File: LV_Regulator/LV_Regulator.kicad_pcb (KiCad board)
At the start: 4 copper layers, 150 x 100 mm, 204 parts, among them IC1 UCC12040DVE, IC2 MIC29152WU, IC3 MIC29152WU, J1 430450400, J2 430450400, J3 430450800, J4 430450800, J5 SWD, J6 2169890001, K1 41.52.9.005.0010, Q1 BC807, U1 ADM2483xRW, U2 STM32F103C8Tx, U3 25CSM04xxSN, U4 BQ25858QWRRVRQ1, U5 CSD19506KTT, U6 CSD19506KTT, U7 CSD19506KTT, U8 CSD19506KTT, Y1 32.768kHz, Y2 8MHz

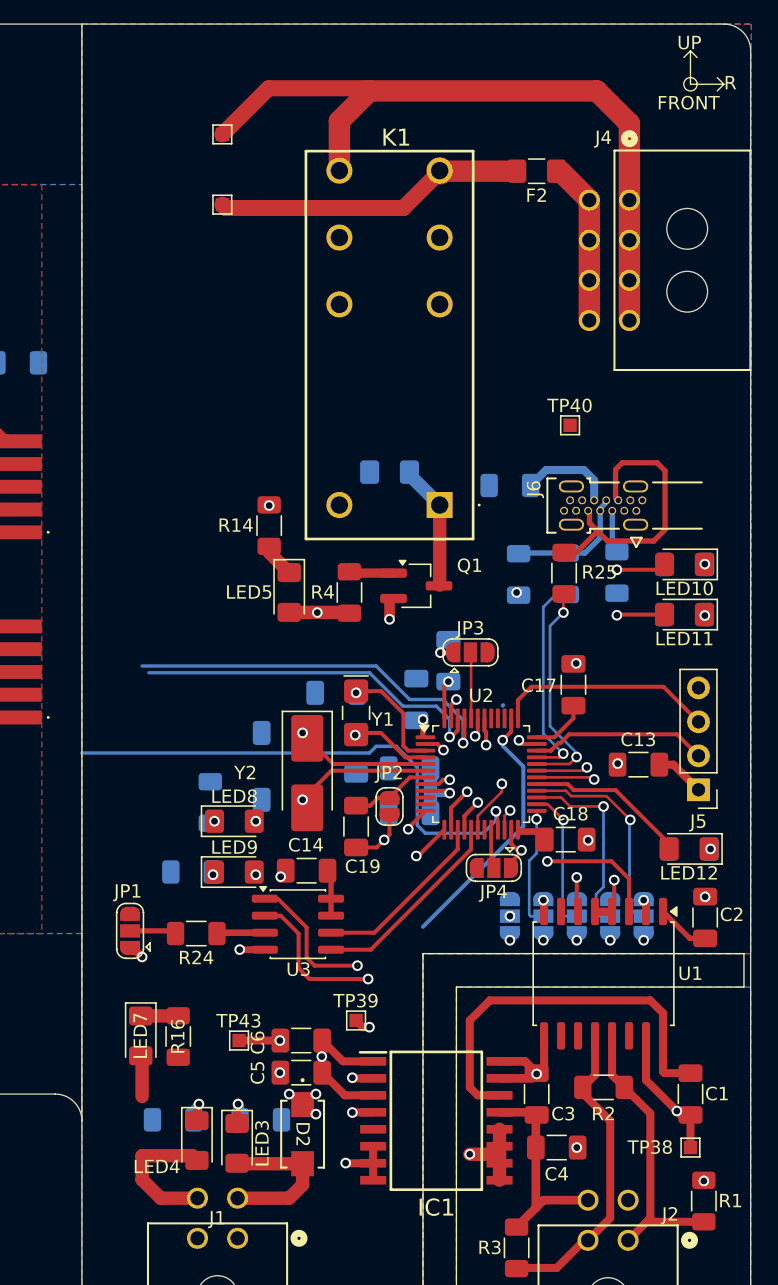
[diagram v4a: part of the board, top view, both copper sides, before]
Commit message: Small corrections to the control part of LV_Regulatoe
Changes to the PCB.
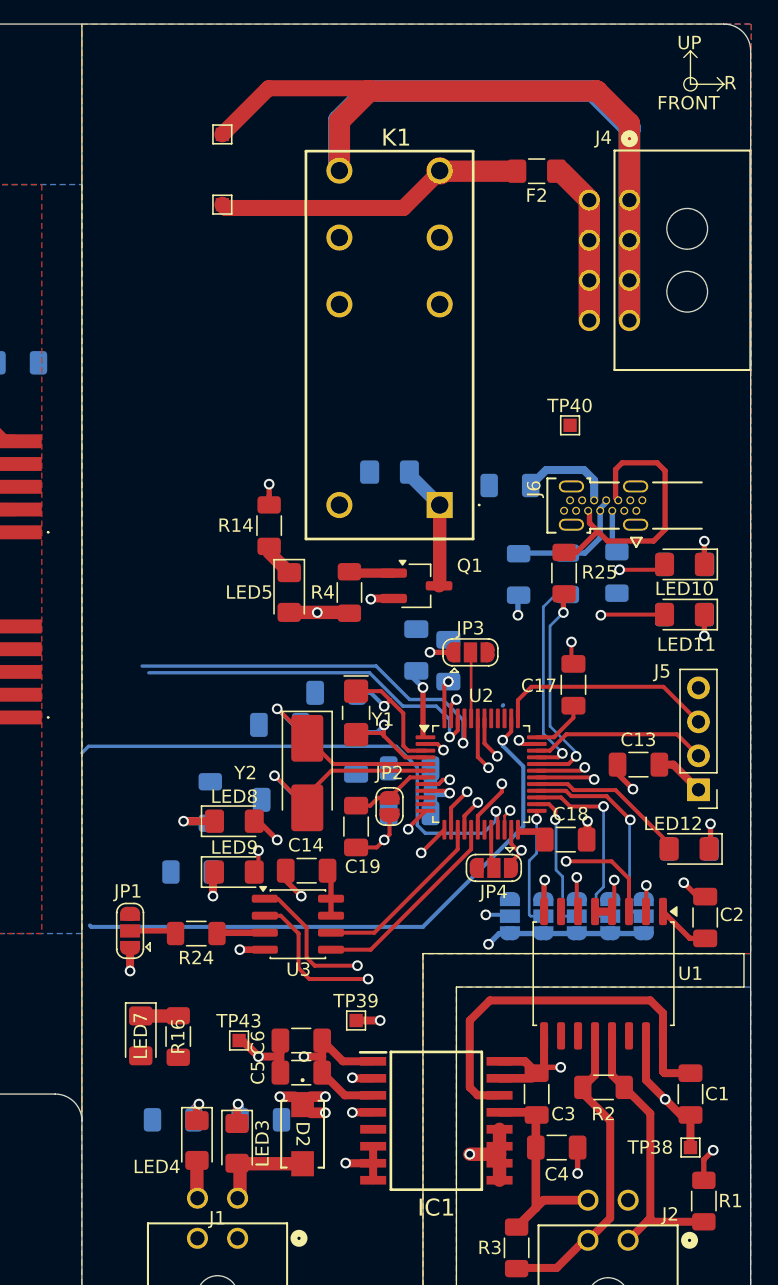
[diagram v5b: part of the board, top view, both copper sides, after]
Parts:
- moved C25 3.70 mm to (206.0, 90.8)
- moved C21 0.63 mm to (195.8, 96.4)
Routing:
- net BAT-: track 54.6 -> 96.6 mm
- net CE_N: track 21.5 -> 46.4 mm
- net GND: track 41.6 -> 63.2 mm, vias 27 -> 26
- net VBAT: track 47.4 -> 62.1 mm, vias 9 -> 5
- net 3V3_EXT: track 10.8 -> 2.84 mm
- net +5V: track 13.0 -> 20.3 mm
- net GND_ISO: track 25.3 -> 31.7 mm
- net HSC_OUT: track 10.6 -> 16.9 mm
- net HSC_IN: track 9.63 -> 15.5 mm
- net 5V_EXT: track 11.8 -> 7.33 mm
- net Net-(LED8-K): track 0.00 -> 4.37 mm
- net Net-(LED9-K): track 0.00 -> 3.67 mm
- net LSC_OUT: track 6.00 -> 9.15 mm
- net LSC_IN: track 8.46 -> 11.5 mm
- net ADR1: track 9.53 -> 12.0 mm
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
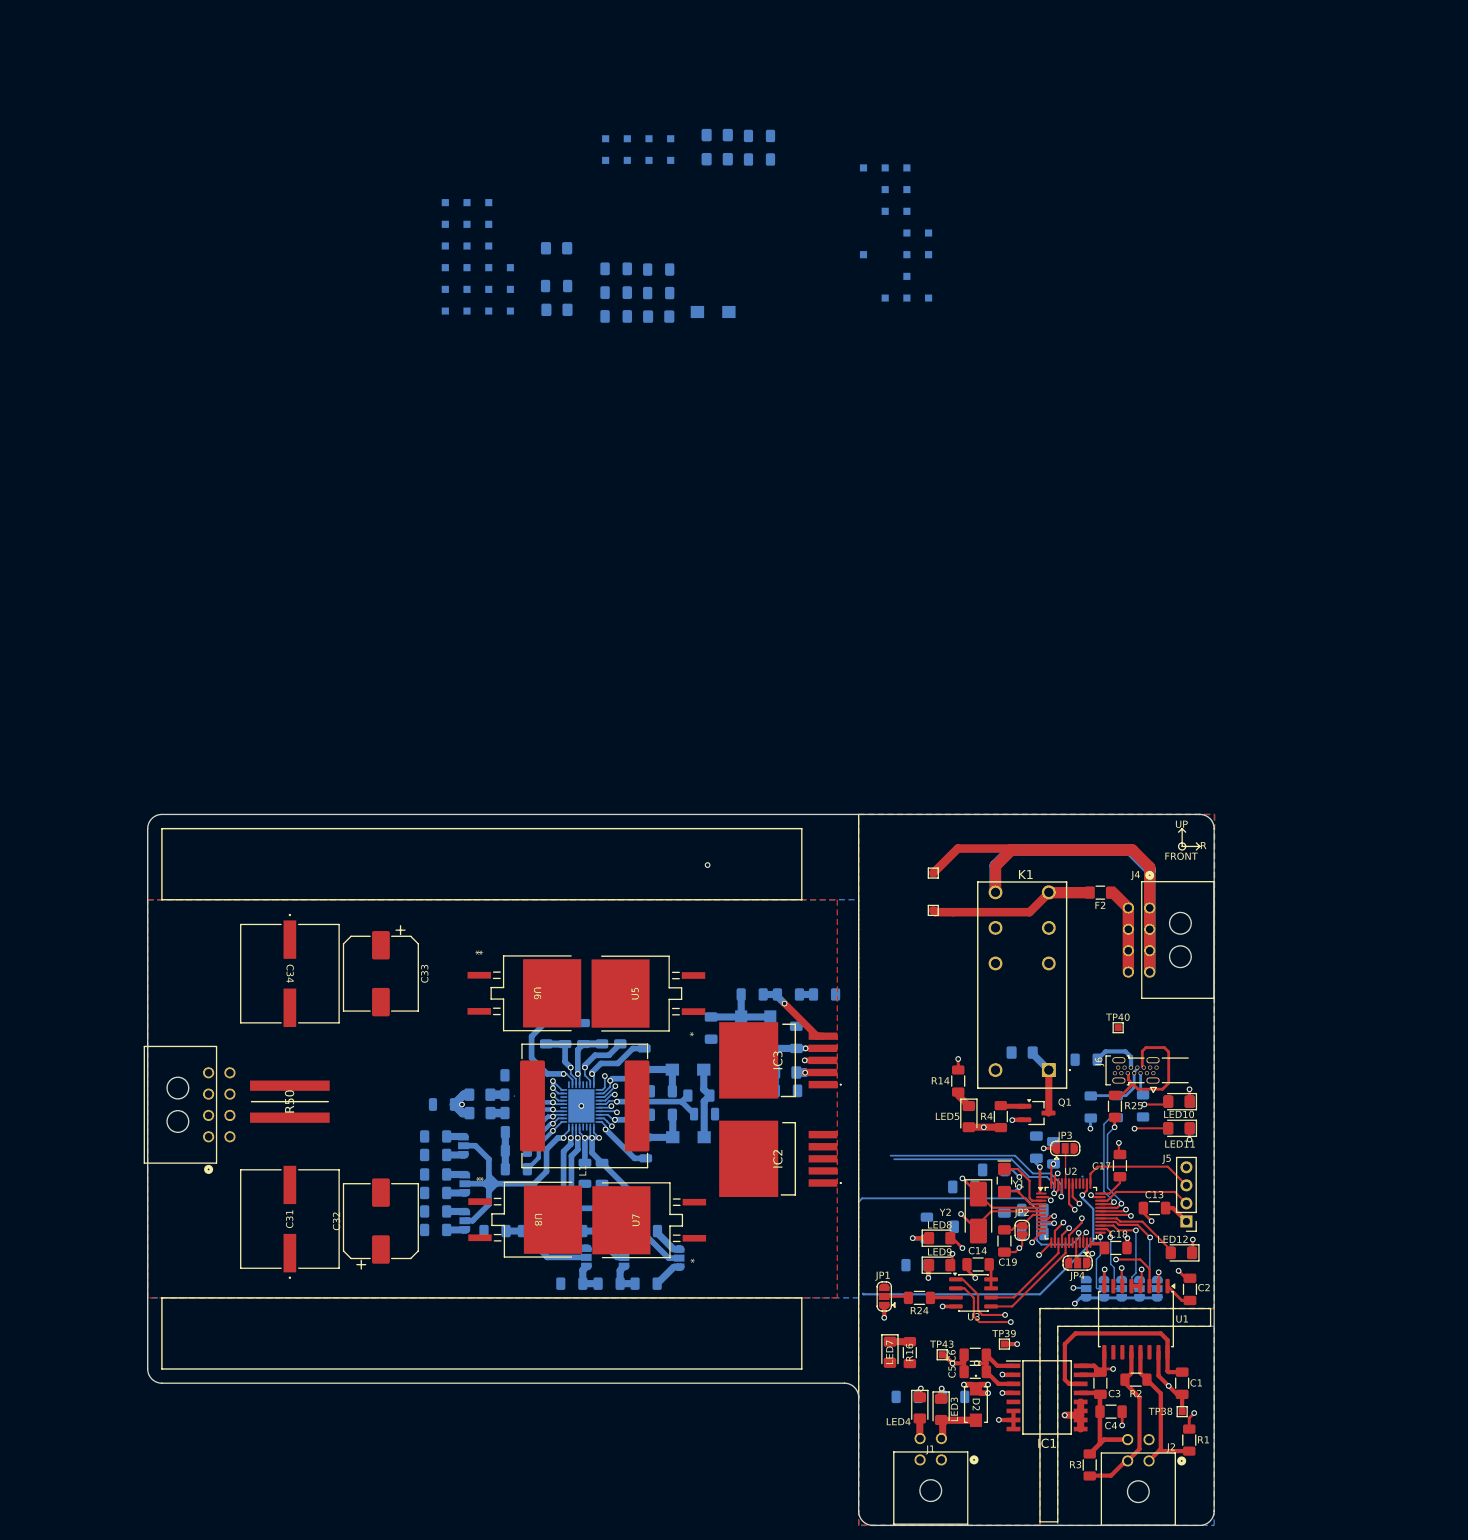
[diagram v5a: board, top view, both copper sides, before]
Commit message: PCB Routing
Did some PCB Routing, added components for 5V Logic regulator, some routing around the BQ25858 IC, will probably need clean up.
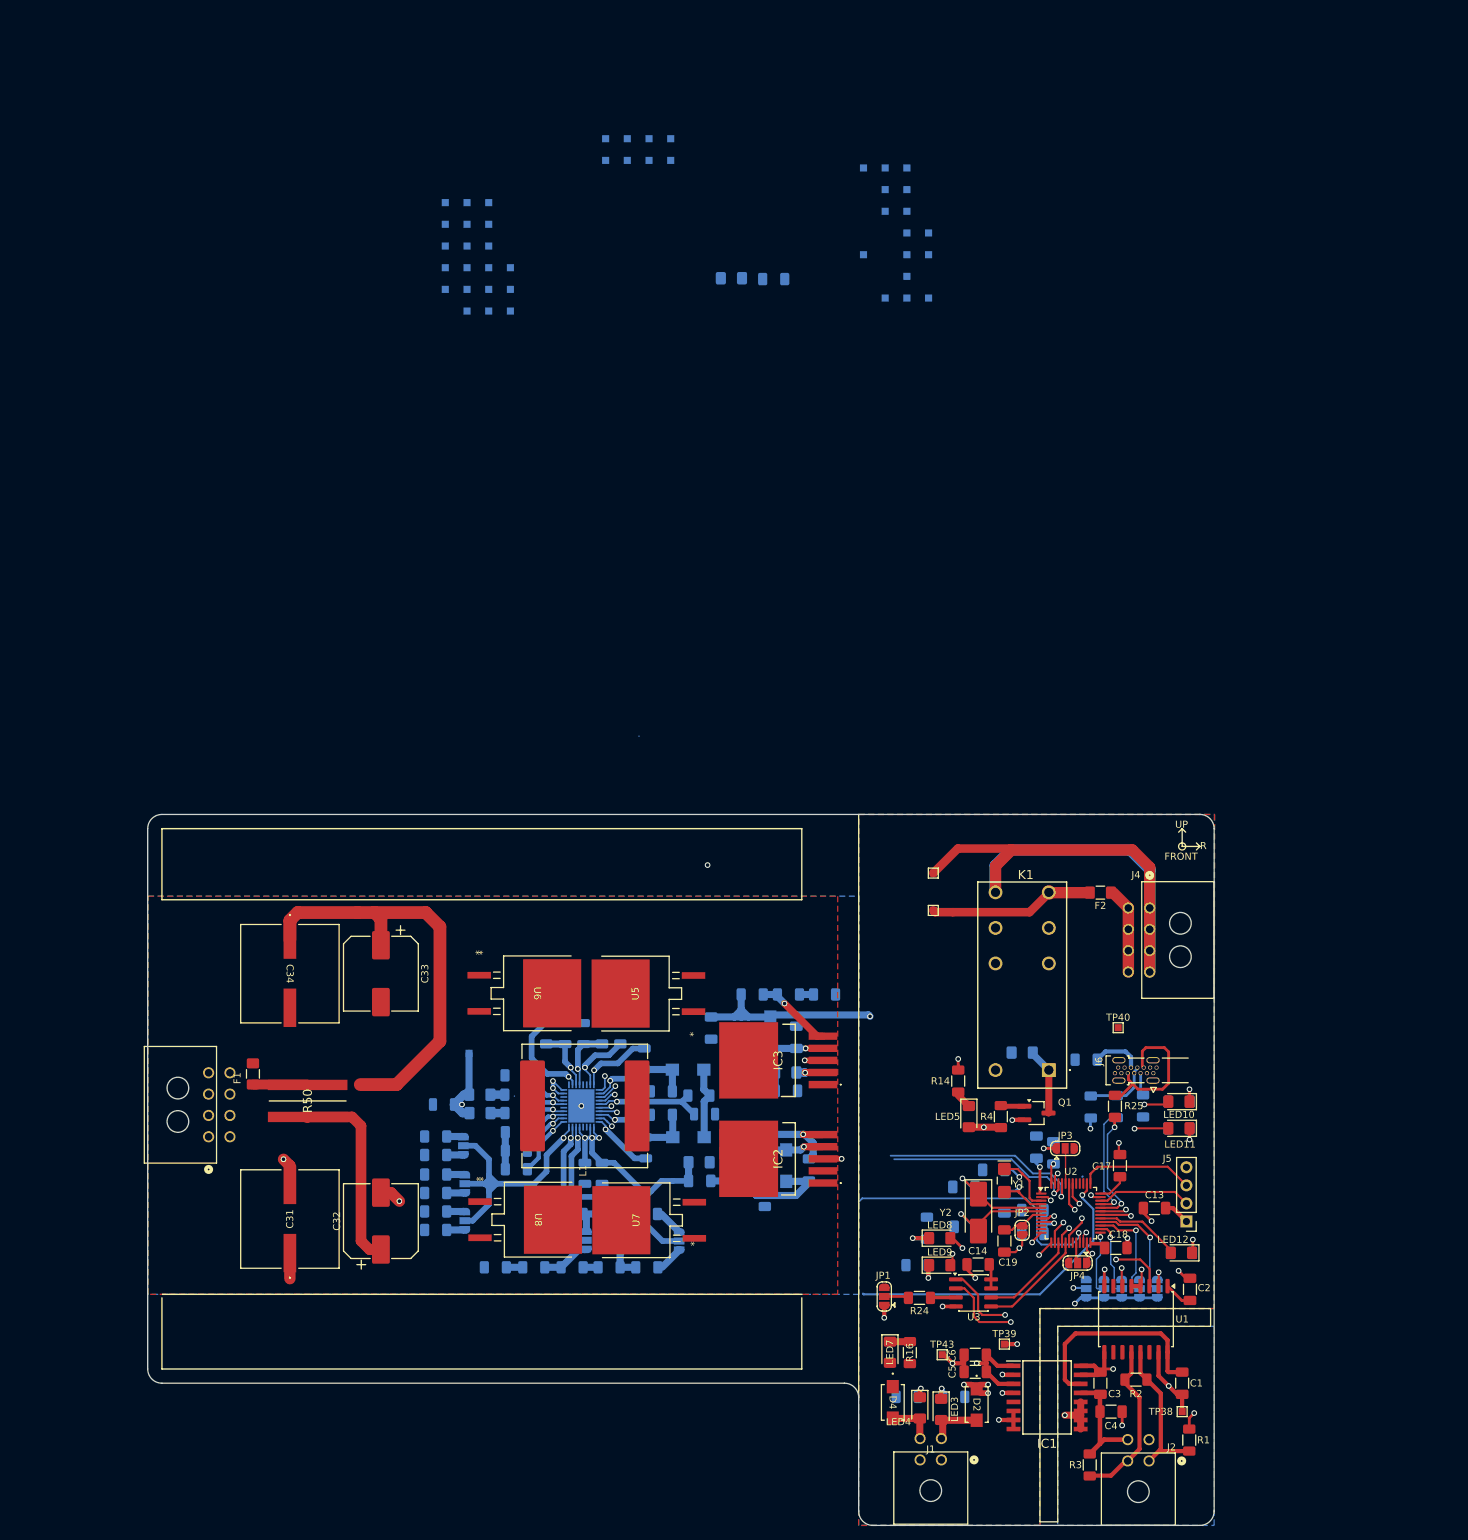
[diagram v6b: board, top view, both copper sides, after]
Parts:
- D4, F1: moved to F.Cu
- moved R10 145.7 mm to (167.8, 97.6), turned to -90 degrees
- moved LED1 140.9 mm to (167.8, 92.6), turned to 90 degrees
- moved C8 126.1 mm to (163.8, 95.5)
- moved C9 125.5 mm to (163.6, 91.6)
- moved R5 125.1 mm to (174.0, 94.0), turned to -90 degrees
- moved F1 123.7 mm to (95.8, 80.5), turned to 90 degrees
- moved C7 122.2 mm to (158.6, 95.5), turned to 180 degrees
- moved R6 122.1 mm to (163.6, 89.0)
- moved D3 120.5 mm to (170.8, 93.4), turned to 90 degrees
- moved F3 119.1 mm to (158.6, 92.9), turned to 180 degrees
- moved R11 111.4 mm to (163.0, 78.3), turned to 90 degrees
- moved LED2 108.7 mm to (165.4, 78.4), turned to 90 degrees
- moved TP1 104.5 mm to (126.2, 77.6)
- moved D4 56.2 mm to (185.8, 126.7)
- moved R15 20.2 mm to (169.1, -31.3)
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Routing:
- net VOUT: track 13.7 -> 81.2 mm
- net REGN: track 8.36 -> 38.9 mm
- net Net-(U6-D): track 0.00 -> 27.7 mm
- net VBAT: track 62.1 -> 79.2 mm, vias 5 -> 6
- net Net-(IC2-ADJ): track 0.00 -> 15.2 mm, vias 0 -> 1
- net +5V: track 20.3 -> 34.5 mm
- net SYS: track 36.2 -> 49.5 mm
- net GND: track 63.2 -> 75.3 mm, vias 26 -> 29
- net 5V_INT: track 0.00 -> 11.6 mm, vias 0 -> 1
- net ACOV: track 26.9 -> 18.3 mm
- net CE_N: track 46.4 -> 51.3 mm
- net 3V3_EXT: track 2.84 -> 6.66 mm
- net 3V3_INT: track 7.41 -> 10.6 mm
- net Net-(LED2-K): track 0.00 -> 2.40 mm
- net Net-(LED1-K): track 0.00 -> 1.96 mm
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
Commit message: PCB Routing progress
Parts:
- moved LED6 72.4 mm to (179.5, 39.1)
- moved R15 72.4 mm to (185.5, 39.2)
- moved TP2 40.3 mm to (163.1, -26.8)
- moved TP3 40.3 mm to (163.1, -29.9)
- moved TP5 40.3 mm to (163.1, -32.9)
- moved TP7 40.3 mm to (163.1, -36.0)
- moved TP8 40.3 mm to (163.1, -39.0)
- moved TP10 40.3 mm to (166.1, -26.8)
- moved TP13 40.3 mm to (166.1, -29.9)
- moved TP14 40.3 mm to (166.1, -32.9)
- moved TP15 40.3 mm to (166.1, -36.0)
- moved TP27 40.3 mm to (166.1, -39.0)
- moved TP30 40.3 mm to (169.2, -23.8)
- moved TP31 40.3 mm to (169.2, -26.8)
- moved TP33 40.3 mm to (169.2, -29.9)
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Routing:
- net VOUT: track 81.2 -> 17.4 mm
- net VBAT: track 79.2 -> 121.3 mm, vias 6 -> 8
- net HIDRV2_FET4: track 2.58 -> 32.4 mm
- net Net-(IC2-IN): track 0.00 -> 26.6 mm, vias 0 -> 1
- net SYS: track 49.5 -> 71.0 mm, vias 3 -> 5
- net GND: track 75.3 -> 93.2 mm
- net LODRV2_FET3: track 2.94 -> 20.5 mm
- net Net-(U6-D): track 27.7 -> 11.8 mm
- net INT_N: track 45.0 -> 39.7 mm
- net HIDRV1_FET1: track 2.27 -> 3.29 mm
- net SW1: track 8.99 -> 9.51 mm
- added copper zone on F.Cu, net Net-(F1-Pad2)
- added copper zone on F.Cu, net VOUT
